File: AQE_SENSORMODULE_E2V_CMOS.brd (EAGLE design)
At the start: 31.2 x 47.5 mm, 35 parts, among them J1 440055-4, J2 AVR_SPI_PRG_6NS, U1 V_REG_LDOSMD, U2 V_REG_LDOSMD, U3 MCP41XXX

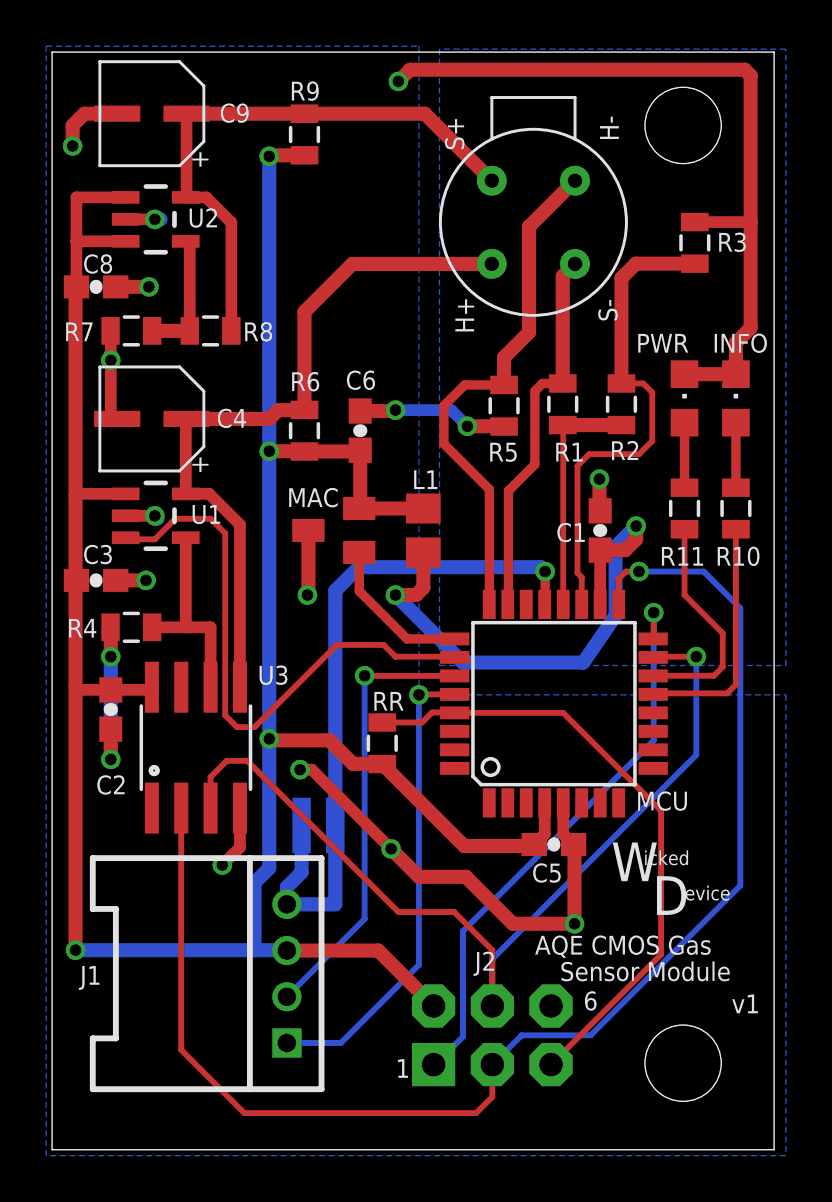
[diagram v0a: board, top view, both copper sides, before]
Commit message: incorporated several changes based on review comments
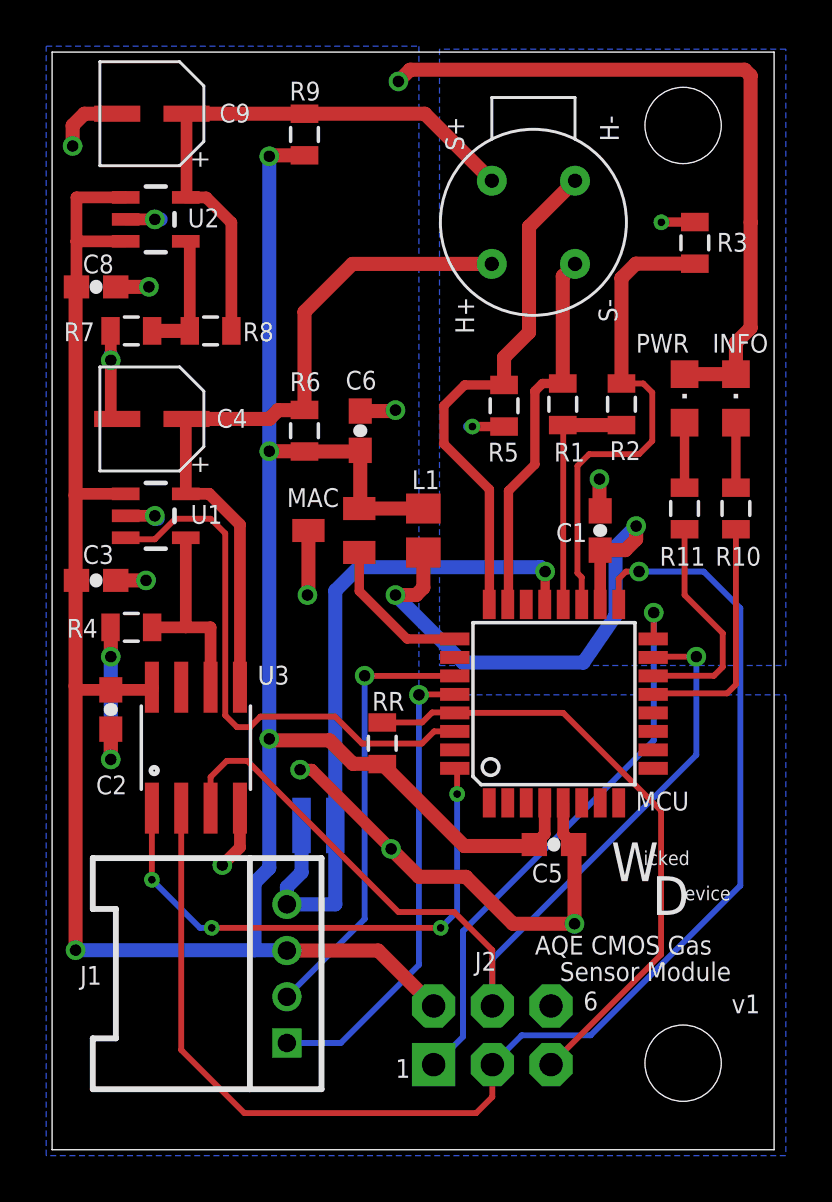
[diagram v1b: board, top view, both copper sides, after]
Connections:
- net /POT_CS: now also MCU.32
- net AGND: now also R3.1, R5.1
- net GND: no longer R3.1, R5.1
- net HEATER_EN: now also MCU.30; no longer MCU.26
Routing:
- net /POT_CS: track 0.00 -> 23.8 mm, vias 0 -> 4
- net GND: track 87.2 -> 79.8 mm, vias 16 -> 15
- net AGND: track 22.3 -> 25.3 mm, vias 2 -> 4
- net HEATER_EN: track 24.7 -> 23.9 mm
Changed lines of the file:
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@@
 <via x="10.7315" y="16.4465" extent="1-16" drill="0.5"/>
 <wire x1="10.7315" y1="16.4465" x2="10.6045" y2="16.4465" width="0.508" layer="16"/>
-<contactref element="R3" pad="1"/>
-<contactref element="R5" pad="1"/>
-<wire x1="19.558" y1="31.2945" x2="19.547" y2="31.3055" width="0.6096" layer="1"/>
-<wire x1="19.547" y1="31.3055" x2="17.9705" y2="31.3055" width="0.6096" layer="1"/>
-<via x="17.9705" y="31.3055" extent="1-16" drill="0.5"/>
-<wire x1="14.859" y1="32.004" x2="17.272" y2="32.004" width="0.508" layer="16"/>
-<wire x1="17.272" y1="32.004" x2="17.9705" y2="31.3055" width="0.508" layer="16"/>
-<wire x1="27.813" y1="40.143" x2="30.215" y2="40.143" width="0.508" layer="1"/>
 <wire x1="30.215" y1="40.143" x2="30.226" y2="40.132" width="0.508" layer="1"/>
 </signal>
@@
 <signal name="/POT_CS">
 <contactref element="U3" pad="1"/>
+<contactref element="MCU" pad="32"/>
+<wire x1="17.4244" y1="16.504" x2="17.526" y2="16.504" width="0.254" layer="1"/>
+<wire x1="17.526" y1="16.504" x2="17.526" y2="15.3924" width="0.254" layer="1"/>
+<via x="17.526" y="15.3924" extent="1-16" drill="0.3302"/>
+<via x="16.8148" y="9.6012" extent="1-16" drill="0.3302"/>
+<wire x1="16.8148" y1="9.6012" x2="6.9088" y2="9.6012" width="0.254" layer="1"/>
+<via x="6.9088" y="9.6012" extent="1-16" drill="0.3302"/>
+<wire x1="6.9088" y1="9.6012" x2="6.4008" y2="9.6012" width="0.254" layer="16"/>
+<wire x1="6.4008" y1="9.6012" x2="4.318" y2="11.684" width="0.254" layer="16"/>
+<via x="4.318" y="11.684" extent="1-16" drill="0.3302"/>
+<wire x1="4.318" y1="11.684" x2="4.318" y2="14.7828" width="0.254" layer="1"/>
+<wire x1="17.526" y1="15.3924" x2="17.526" y2="10.3124" width="0.254" layer="16"/>
+<wire x1="17.526" y1="10.3124" x2="16.8148" y2="9.6012" width="0.254" layer="16"/>
 </signal>
 <signal name="AGND">
@@
 <wire x1="13.2715" y1="25.2095" x2="21.1455" y2="25.2095" width="0.6096" layer="16"/>
 <wire x1="21.1455" y1="25.2095" x2="21.336" y2="25.019" width="0.6096" layer="16"/>
+<contactref element="R3" pad="1"/>
+<contactref element="R5" pad="1"/>
+<wire x1="19.558" y1="31.2945" x2="18.1864" y2="31.2945" width="0.4064" layer="1"/>
+<wire x1="18.1864" y1="31.2945" x2="18.1864" y2="31.2928" width="0.4064" layer="1"/>
+<via x="18.1864" y="31.2928" extent="1-16" drill="0.3302"/>
+<wire x1="18.1864" y1="31.2928" x2="17.9832" y2="31.2928" width="0.4064" layer="16"/>
+<wire x1="27.813" y1="40.143" x2="26.3652" y2="40.143" width="0.4064" layer="1"/>
+<wire x1="26.3652" y1="40.143" x2="26.3652" y2="40.132" width="0.4064" layer="1"/>
+<via x="26.3652" y="40.132" extent="1-16" drill="0.3302"/>
 </signal>
 <signal name="STATUS">
@@
 <signal name="HEATER_EN">
 <contactref element="U1" pad="3"/>
-<contactref element="MCU" pad="26"/>
-<wire x1="17.4244" y1="21.304" x2="17.3924" y2="21.336" width="0.254" layer="1"/>
-<wire x1="17.3924" y1="21.336" x2="14.859" y2="21.336" width="0.254" layer="1"/>
-<wire x1="14.859" y1="21.336" x2="14.351" y2="21.844" width="0.254" layer="1"/>
-<wire x1="14.351" y1="21.844" x2="12.319" y2="21.844" width="0.254" layer="1"/>
-<wire x1="12.319" y1="21.844" x2="8.763" y2="18.288" width="0.254" layer="1"/>
-<wire x1="8.763" y1="18.288" x2="8.001" y2="18.288" width="0.254" layer="1"/>
+<wire x1="8.5598" y1="18.288" x2="8.001" y2="18.288" width="0.254" layer="1"/>
 <wire x1="8.001" y1="18.288" x2="7.493" y2="18.796" width="0.254" layer="1"/>
 <wire x1="7.493" y1="18.796" x2="7.493" y2="26.67" width="0.254" layer="1"/>
@@
 <wire x1="4.445" y1="26.416" x2="3.252" y2="26.416" width="0.254" layer="1"/>
 <wire x1="3.252" y1="26.416" x2="3.186" y2="26.482" width="0.254" layer="1"/>
+<contactref element="MCU" pad="30"/>
+<wire x1="8.5598" y1="18.288" x2="9.017" y2="18.7452" width="0.254" layer="1"/>
+<wire x1="9.017" y1="18.7452" x2="12.2428" y2="18.7452" width="0.254" layer="1"/>
+<wire x1="12.2428" y1="18.7452" x2="13.4112" y2="17.5768" width="0.254" layer="1"/>
+<wire x1="16.002" y1="17.5768" x2="16.5292" y2="18.104" width="0.254" layer="1"/>
+<wire x1="16.5292" y1="18.104" x2="17.4244" y2="18.104" width="0.254" layer="1"/>
+<wire x1="13.4112" y1="17.5768" x2="16.002" y2="17.5768" width="0.254" layer="1"/>
 </signal>
 <signal name="RETURN_GND">
@@
 </signal>
 </signals>
-<errors>
-</errors>
 </board>
 </drawing>

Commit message: updated schematic and board to make attiny48 pinout compatible with egg shield
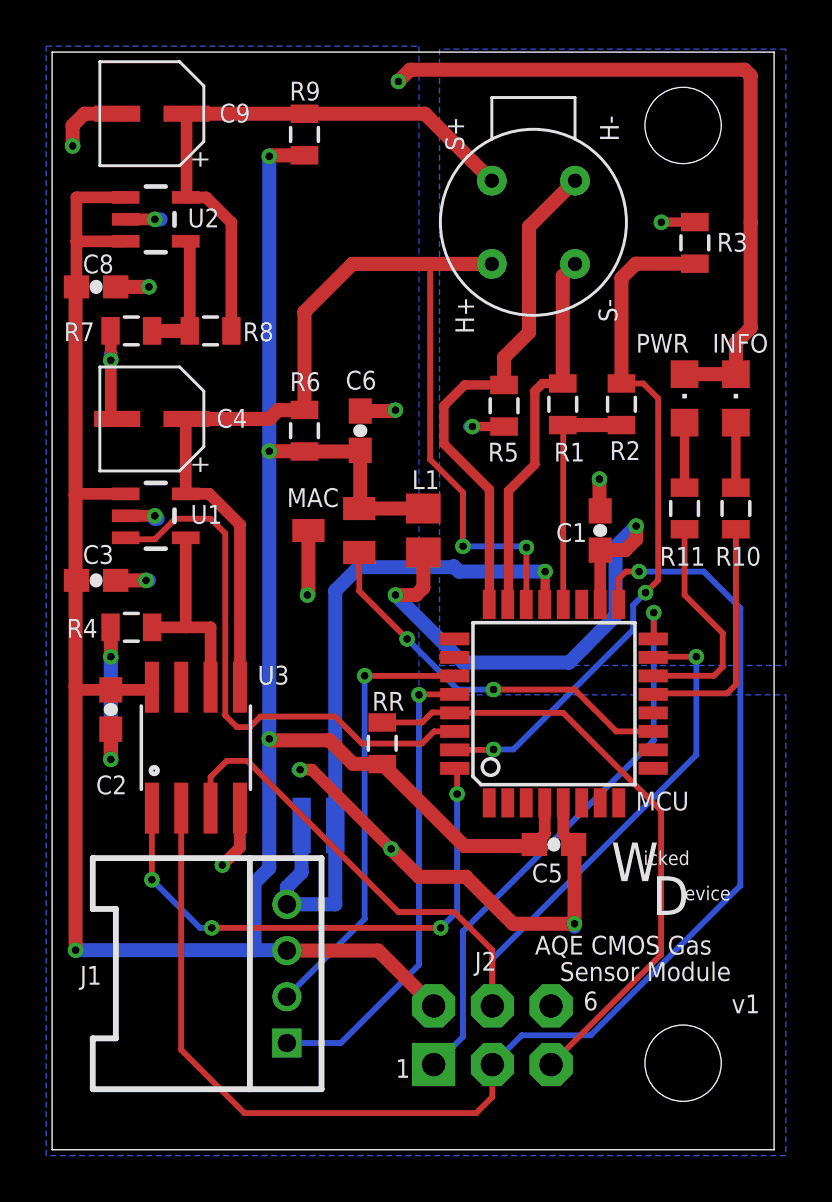
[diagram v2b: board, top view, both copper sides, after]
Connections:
- net /R2_SEL: now also MCU.31; no longer MCU.19
- net HEATER_VCC: now also MCU.22
- net MAC_IO: now also MCU.11; no longer MCU.25
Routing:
- net HEATER_VCC: track 31.7 -> 49.7 mm, vias 0 -> 2
- net MAC_IO: track 6.67 -> 16.9 mm, vias 0 -> 2
- net /R2_SEL: track 21.3 -> 30.2 mm, vias 0 -> 2

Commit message: updated files
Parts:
- C1, C2, C3, C5, C6, C8: device SparkFun:0603-CAP -> SparkFun-Passives:0805
- R11: value 470ohm -> 270ohm
- R5: value (none) -> 10R
- renumbered U$4 to GAS
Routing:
- net GND: track 79.8 -> 78.4 mm
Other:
- outline, holes or cut-outs redrawn
- board text added: "MCP4151"
- board text added: "Tiny48/88"
- board text added: "v1.2"
- board text removed: "v1"

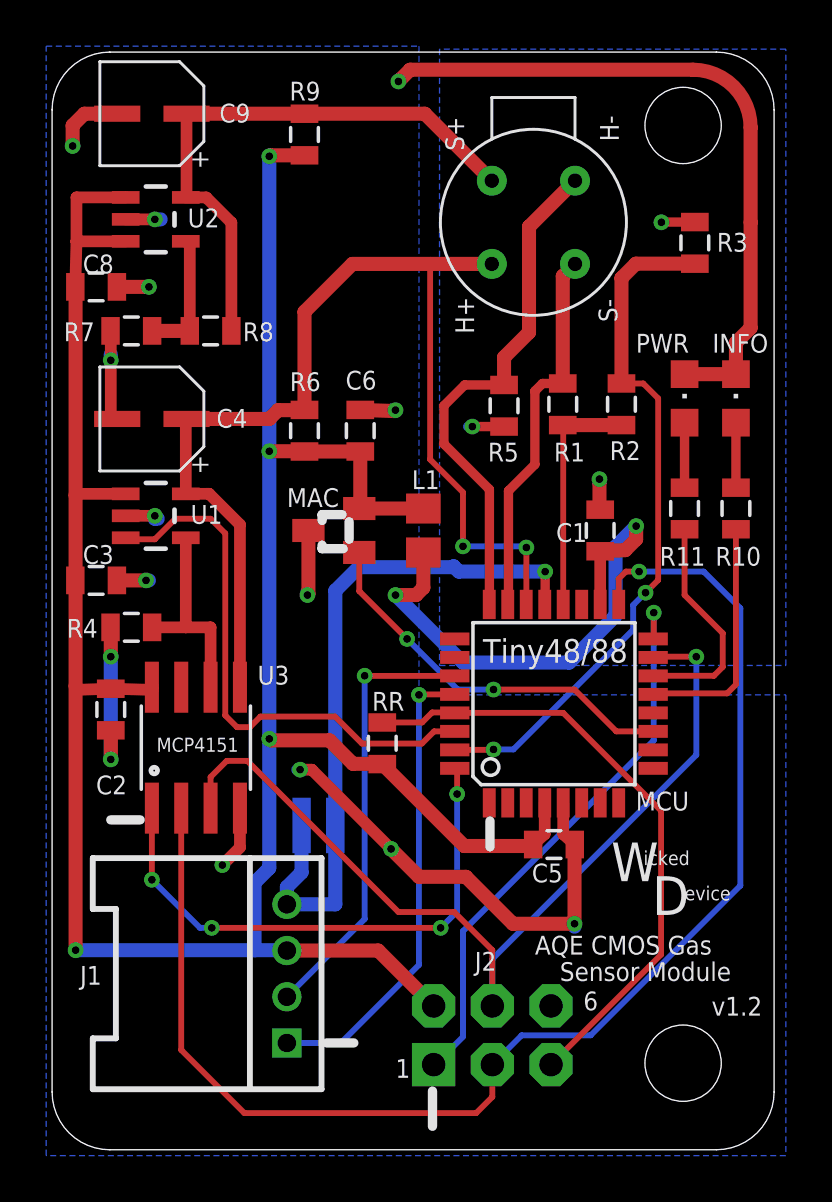
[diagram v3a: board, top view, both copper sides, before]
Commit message: flipped J1 connector pinout around by 180 degrees
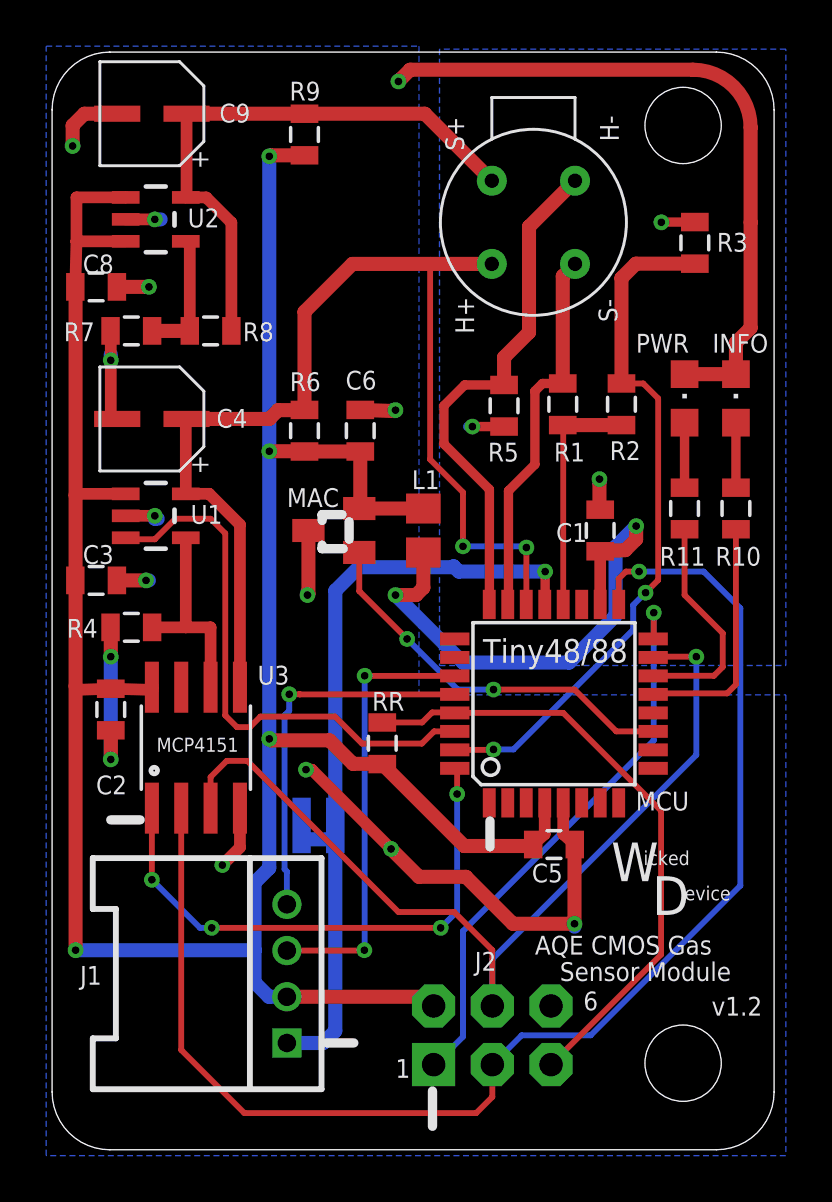
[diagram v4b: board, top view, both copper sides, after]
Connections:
- net RETURN_GND: now also J1.1; no longer J1.4
- net SCL: now also J1.4; no longer J1.1
- net SDA: now also J1.3; no longer J1.2
- net VCC: now also J1.2; no longer J1.3
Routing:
- net RETURN_GND: track 7.99 -> 12.1 mm
- net SCL: track 20.4 -> 16.4 mm
- net VCC: track 120.2 -> 121.0 mm
- net SDA: vias 1 -> 2
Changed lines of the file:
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@@
 <wire x1="7.366" y1="12.319" x2="7.493" y2="12.446" width="0.508" layer="16"/>
 <wire x1="14.6685" y1="13.0175" x2="11.2395" y2="16.4465" width="0.508" layer="1"/>
-<wire x1="11.2395" y1="16.4465" x2="10.7315" y2="16.4465" width="0.508" layer="1"/>
-<via x="10.7315" y="16.4465" extent="1-16" drill="0.3302"/>
-<wire x1="10.7315" y1="16.4465" x2="10.6045" y2="16.4465" width="0.508" layer="16"/>
+<wire x1="11.2395" y1="16.4465" x2="10.9855" y2="16.4465" width="0.508" layer="1"/>
+<via x="10.9855" y="16.4465" extent="1-16" drill="0.3302"/>
 <wire x1="30.215" y1="40.143" x2="30.226" y2="40.132" width="0.508" layer="1"/>
 <wire x1="15.494" y1="46.736" x2="27.726" y2="46.736" width="0.6096" layer="1"/>
@@
 <signal name="VCC">
 <contactref element="C3" pad="2"/>
-<contactref element="J1" pad="3"/>
 <contactref element="R6" pad="1"/>
 <contactref element="J2" pad="2"/>
@@
 <wire x1="13.335" y1="30.215" x2="13.292" y2="30.222" width="0.4064" layer="1"/>
 <wire x1="13.335" y1="30.215" x2="10.922" y2="30.215" width="0.6096" layer="1"/>
-<wire x1="10.16" y1="8.62" x2="14.113" y2="8.62" width="0.6096" layer="1"/>
-<wire x1="14.113" y1="8.62" x2="16.51" y2="6.223" width="0.6096" layer="1"/>
 <contactref element="U1" pad="1"/>
 <wire x1="13.292" y1="27.747" x2="13.335" y2="27.747" width="0.6096" layer="1"/>
@@
 <wire x1="1.016" y1="8.636" x2="1.016" y2="20.066" width="0.6096" layer="1"/>
 <wire x1="1.016" y1="20.066" x2="1.016" y2="24.638" width="0.6096" layer="1"/>
-<wire x1="10.16" y1="8.62" x2="10.16" y2="8.636" width="0.6096" layer="16"/>
-<wire x1="10.16" y1="8.636" x2="8.763" y2="8.636" width="0.6096" layer="16"/>
 <via x="1.016" y="8.636" extent="1-16" drill="0.3302"/>
 <wire x1="8.763" y1="8.636" x2="1.016" y2="8.636" width="0.6096" layer="16"/>
@@
 <wire x1="3.186" y1="39.309" x2="1.055" y2="39.309" width="0.508" layer="1"/>
 <wire x1="1.055" y1="39.309" x2="1.055" y2="39.3065" width="0.508" layer="1"/>
+<contactref element="J1" pad="2"/>
+<wire x1="16.51" y1="6.223" x2="16.113" y2="6.62" width="0.6096" layer="1"/>
+<wire x1="16.113" y1="6.62" x2="10.16" y2="6.62" width="0.6096" layer="1"/>
+<wire x1="10.16" y1="6.62" x2="9.382" y2="6.62" width="0.6096" layer="16"/>
+<wire x1="9.382" y1="6.62" x2="8.763" y2="7.239" width="0.6096" layer="16"/>
+<wire x1="8.763" y1="7.239" x2="8.763" y2="8.636" width="0.6096" layer="16"/>
 </signal>
 <signal name="/RESET">
@@
 </signal>
 <signal name="SDA">
-<contactref element="J1" pad="2"/>
 <contactref element="MCU" pad="27"/>
 <wire x1="17.4244" y1="20.504" x2="13.532" y2="20.504" width="0.254" layer="1"/>
 <wire x1="13.532" y1="20.504" x2="13.5255" y2="20.5105" width="0.4064" layer="1"/>
 <via x="13.5255" y="20.5105" extent="1-16" drill="0.3302"/>
-<wire x1="13.5255" y1="20.5105" x2="13.5255" y2="9.9855" width="0.254" layer="16"/>
-<wire x1="13.5255" y1="9.9855" x2="10.16" y2="6.62" width="0.254" layer="16"/>
+<wire x1="13.5255" y1="20.5105" x2="13.5255" y2="8.636" width="0.254" layer="16"/>
+<contactref element="J1" pad="3"/>
+<wire x1="13.5255" y1="8.636" x2="13.5128" y2="8.636" width="0.254" layer="16"/>
+<via x="13.5128" y="8.636" extent="1-16" drill="0.3302"/>
+<wire x1="13.5128" y1="8.636" x2="13.5128" y2="8.62" width="0.254" layer="1"/>
+<wire x1="13.5128" y1="8.62" x2="10.16" y2="8.62" width="0.254" layer="1"/>
 </signal>
 <signal name="SCL">
-<contactref element="J1" pad="1"/>
 <contactref element="MCU" pad="28"/>
-<wire x1="17.4244" y1="19.704" x2="15.894" y2="19.704" width="0.254" layer="1"/>
-<wire x1="15.894" y1="19.704" x2="15.875" y2="19.685" width="0.4064" layer="1"/>
-<via x="15.875" y="19.685" extent="1-16" drill="0.3302"/>
-<wire x1="15.875" y1="19.685" x2="15.875" y2="8.001" width="0.254" layer="16"/>
-<wire x1="15.875" y1="8.001" x2="12.494" y2="4.62" width="0.254" layer="16"/>
-<wire x1="12.494" y1="4.62" x2="10.16" y2="4.62" width="0.254" layer="16"/>
+<contactref element="J1" pad="4"/>
+<wire x1="17.4244" y1="19.704" x2="10.7188" y2="19.704" width="0.254" layer="1"/>
+<via x="10.2616" y="19.7104" extent="1-16" drill="0.3302"/>
+<wire x1="10.0584" y1="18.796" x2="10.0584" y2="12.1412" width="0.254" layer="16"/>
+<wire x1="10.0584" y1="12.1412" x2="10.16" y2="12.0396" width="0.254" layer="16"/>
+<wire x1="10.16" y1="12.0396" x2="10.16" y2="10.62" width="0.254" layer="16"/>
+<wire x1="10.7188" y1="19.704" x2="10.7124" y2="19.7104" width="0.254" layer="1"/>
+<wire x1="10.7124" y1="19.7104" x2="10.2616" y2="19.7104" width="0.254" layer="1"/>
+<wire x1="10.2616" y1="19.7104" x2="10.2616" y2="18.9992" width="0.254" layer="16"/>
+<wire x1="10.2616" y1="18.9992" x2="10.0584" y2="18.796" width="0.254" layer="16"/>
 </signal>
 <signal name="/R2_SEL">
@@
 </signal>
 <signal name="RETURN_GND">
-<contactref element="J1" pad="4"/>
 <contactref element="U$2" pad="2"/>
 <contactref element="U$3" pad="2"/>
-<wire x1="12.2555" y1="13.4335" x2="12.2555" y2="10.62" width="0.6096" layer="16"/>
-<wire x1="12.2555" y1="10.62" x2="10.16" y2="10.62" width="0.6096" layer="16"/>
-<wire x1="10.16" y1="10.62" x2="10.16" y2="11.3665" width="0.6096" layer="16"/>
-<wire x1="10.795" y1="13.4335" x2="10.795" y2="12.0015" width="0.6096" layer="16"/>
-<wire x1="10.795" y1="12.0015" x2="10.16" y2="11.3665" width="0.6096" layer="16"/>
+<contactref element="J1" pad="1"/>
+<wire x1="10.795" y1="13.4335" x2="12.2555" y2="13.4335" width="0.6096" layer="16"/>
+<wire x1="12.2555" y1="13.4335" x2="12.2555" y2="5.1435" width="0.6096" layer="16"/>
+<wire x1="12.2555" y1="5.1435" x2="11.732" y2="4.62" width="0.6096" layer="16"/>
+<wire x1="11.732" y1="4.62" x2="10.16" y2="4.62" width="0.6096" layer="16"/>
 </signal>
 </signals>
